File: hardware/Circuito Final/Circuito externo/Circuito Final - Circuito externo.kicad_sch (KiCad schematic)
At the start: 0 parts

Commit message: update circuito externo
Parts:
- added J1, J2: Conn_02x19_Odd_Even, Connector_PinSocket_2.54mm:PinSocket_2x19_P2.54mm_Vertical, symbol Connector_Generic:Conn_02x19_Odd_Even
- added J3, J4: Conn_01x02, Connector_PinSocket_2.54mm:PinSocket_1x02_P2.54mm_Vertical, symbol Connector_Generic:Conn_01x02
- added Jsalida_1, Jsalida_2, Jsalida_3, Jsalida_4, Jsalida_5: Conn_02x07_Odd_Even, Connector_IDC:IDC-Header_2x07_P2.54mm_Horizontal, symbol Connector_Generic:Conn_02x07_Odd_Even
- added SW1: SW_SPDT, symbol Switch:SW_SPDT
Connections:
- new net Bit_0: Jsalida_1.2 (Pin_2), Jsalida_2.2 (Pin_2), Jsalida_3.2 (Pin_2), Jsalida_4.2 (Pin_2), Jsalida_5.2 (Pin_2)
- new net Bit_1: Jsalida_1.1 (Pin_1), Jsalida_2.1 (Pin_1), Jsalida_3.1 (Pin_1), Jsalida_4.1 (Pin_1), Jsalida_5.1 (Pin_1)
- new net Bit_2: Jsalida_1.3 (Pin_3), Jsalida_2.3 (Pin_3), Jsalida_3.3 (Pin_3), Jsalida_4.3 (Pin_3), Jsalida_5.3 (Pin_3)
- new net Data_1: Jsalida_1.14 (Pin_14)
- new net Data_2: Jsalida_2.14 (Pin_14)
- new net Data_3: Jsalida_3.14 (Pin_14)
- new net Data_4: Jsalida_4.14 (Pin_14)
- new net Data_5: Jsalida_5.14 (Pin_14)
- new net GND: J1.19 (Pin_19), J1.21 (Pin_21), J1.7 (Pin_7), J3.2 (Pin_2), J4.2 (Pin_2), Jsalida_1.10 (Pin_10), Jsalida_2.10 (Pin_10), Jsalida_3.10 (Pin_10), Jsalida_4.10 (Pin_10), Jsalida_5.10 (Pin_10), SW1.3 (C)
- new net Vcc: J1.17 (Pin_17), SW1.2 (B)
- new net Vcc_out: Jsalida_1.13 (Pin_13), Jsalida_2.13 (Pin_13), Jsalida_3.13 (Pin_13), Jsalida_4.13 (Pin_13), Jsalida_5.13 (Pin_13), SW1.1 (A)
- new net bus_neg_1: Jsalida_1.7 (Pin_7), Jsalida_1.8 (Pin_8)
- new net bus_neg_2: Jsalida_2.7 (Pin_7), Jsalida_2.8 (Pin_8)
- new net bus_neg_3: Jsalida_3.7 (Pin_7), Jsalida_3.8 (Pin_8)
- new net bus_neg_4: Jsalida_4.7 (Pin_7), Jsalida_4.8 (Pin_8)
- new net bus_neg_5: Jsalida_5.7 (Pin_7), Jsalida_5.8 (Pin_8)
- new net bus_pos_1: Jsalida_1.5 (Pin_5), Jsalida_1.6 (Pin_6)
- new net bus_pos_2: Jsalida_2.5 (Pin_5), Jsalida_2.6 (Pin_6)
- new net bus_pos_3: Jsalida_3.5 (Pin_5), Jsalida_3.6 (Pin_6)
- new net bus_pos_4: Jsalida_4.5 (Pin_5), Jsalida_4.6 (Pin_6)
- new net bus_pos_5: Jsalida_5.5 (Pin_5), Jsalida_5.6 (Pin_6)
- new net clk_latch: Jsalida_1.11 (Pin_11), Jsalida_2.11 (Pin_11), Jsalida_3.11 (Pin_11), Jsalida_4.11 (Pin_11), Jsalida_5.11 (Pin_11)
- new net clk_shift: Jsalida_1.9 (Pin_9), Jsalida_2.9 (Pin_9), Jsalida_3.9 (Pin_9), Jsalida_4.9 (Pin_9), Jsalida_5.9 (Pin_9)
- new net reset: Jsalida_1.12 (Pin_12), Jsalida_2.12 (Pin_12), Jsalida_3.12 (Pin_12), Jsalida_4.12 (Pin_12), Jsalida_5.12 (Pin_12)
- new net salida_adc_1: Jsalida_1.4 (Pin_4)
- new net salida_adc_2: Jsalida_2.4 (Pin_4)
- new net salida_adc_3: Jsalida_3.4 (Pin_4)
- new net salida_adc_4: Jsalida_4.4 (Pin_4)
- new net salida_adc_5: Jsalida_5.4 (Pin_4)

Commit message: update pcb externo
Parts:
- removed Jsalida_5: Conn_02x07_Odd_Even, Connector_IDC:IDC-Header_2x07_P2.54mm_Horizontal, symbol Connector_Generic:Conn_02x07_Odd_Even
- added Bornera1: Conn_01x02_Socket, Huellas:TerminalBlock_bornier-2_P5.08mm, symbol Connector:Conn_01x02_Socket
- added C1: 10u, Capacitor_SMD:C_1206_3216Metric_Pad1.33x1.80mm_HandSolder, symbol Device:C
- added J5: Conn_02x04_Counter_Clockwise, Connector_PinHeader_2.54mm:PinHeader_2x04_P2.54mm_Vertical, symbol Connector_Generic:Conn_02x04_Counter_Clockwise
- added TP1, TP2: TestPoint, symbol Connector:TestPoint
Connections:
- net Bit_0: now also J2.1 (Pin_1)
- net Bit_1: now also J2.2 (Pin_2)
- net Bit_2: now also J2.4 (Pin_4)
- net Data_1: now also J1.4 (Pin_4)
- net Data_2: now also J1.24 (Pin_24)
- net GND: now also J1.20 (Pin_20), J2.10 (Pin_10), J2.19 (Pin_19), J2.31 (Pin_31)
- net bus_neg_1: now also Bornera1.1 (Pin_1), C1.2, TP2.1
- net bus_pos_1: now also J5.1 (Pin_1)
- net bus_pos_2: now also J5.2 (Pin_2)
- net bus_pos_3: now also J5.3 (Pin_3)
- net bus_pos_4: now also J5.4 (Pin_4)
- net clk_latch: now also J1.1 (Pin_1)
- net clk_shift: now also J1.2 (Pin_2)
- new net bus_pos_salida: Bornera1.2 (Pin_2), C1.1, J5.5 (Pin_5), J5.6 (Pin_6), J5.7 (Pin_7), J5.8 (Pin_8), TP1.1
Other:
- moved on the sheet: J1, J2, J3, J4, SW1

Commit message: version actualizada del pcb externo
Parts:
- removed J5: Conn_02x04_Counter_Clockwise, Connector_PinHeader_2.54mm:PinHeader_2x04_P2.54mm_Vertical, symbol Connector_Generic:Conn_02x04_Counter_Clockwise
- added SW2: SW_DIP_x04, Button_Switch_THT:SW_DIP_SPSTx04_Slide_9.78x12.34mm_W7.62mm_P2.54mm, symbol Switch:SW_DIP_x04
- SW1: footprint (none) -> Button_Switch_THT:SW_Slide_SPDT_Straight_CK_OS102011MS2Q
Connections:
- net Vcc: now also SW1.1 (A); no longer SW1.2 (B)
- net Vcc_out: now also SW1.2 (B); no longer SW1.1 (A)
- net bus_pos_1: now also SW2.1
- net bus_pos_2: now also SW2.2
- net bus_pos_3: now also SW2.3
- net bus_pos_4: now also SW2.4
- net bus_pos_salida: now also SW2.5, SW2.6, SW2.7, SW2.8
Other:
- moved on the sheet: SW1

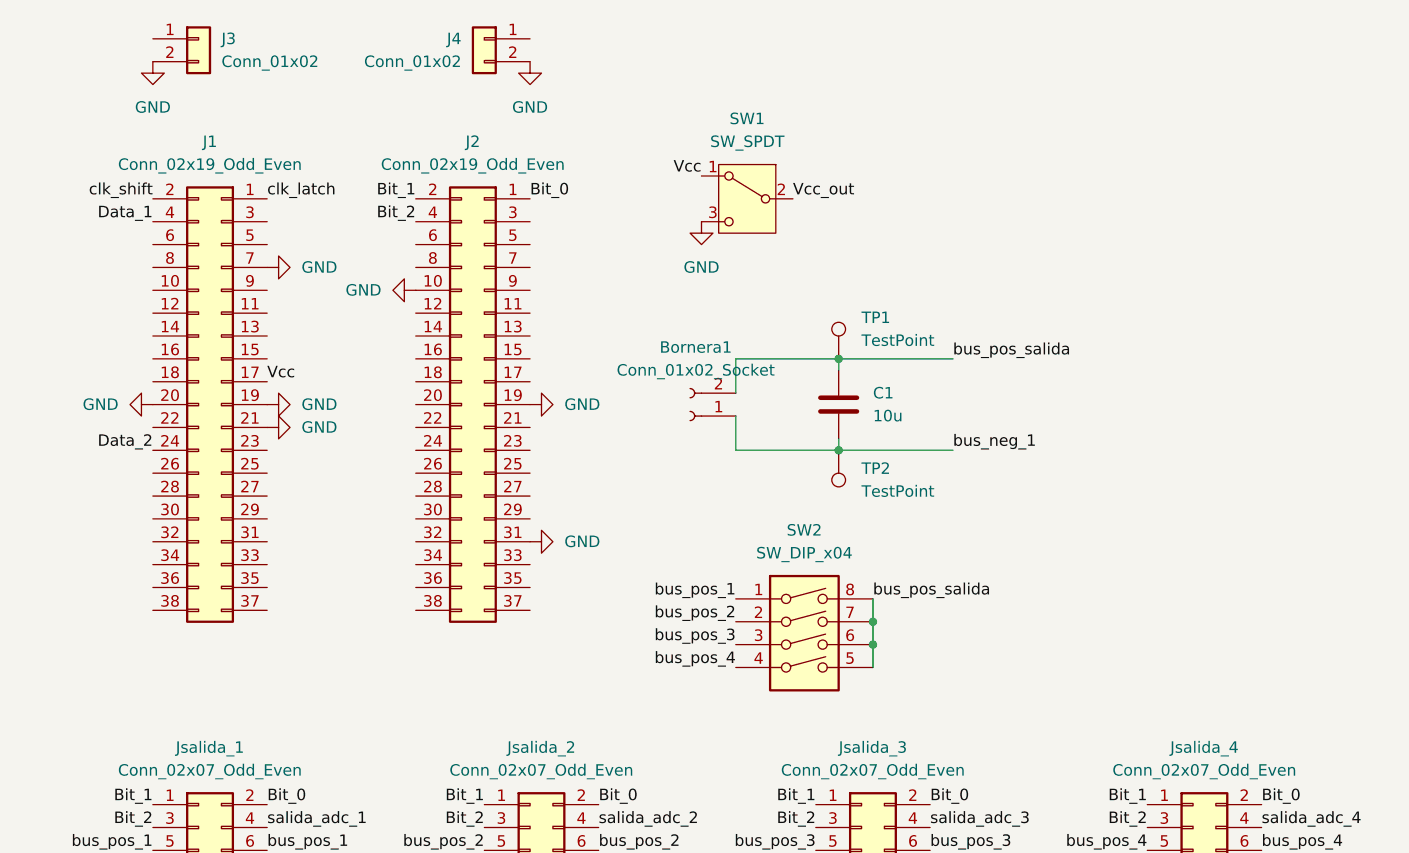
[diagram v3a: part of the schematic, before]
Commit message: update pcb circuito externo
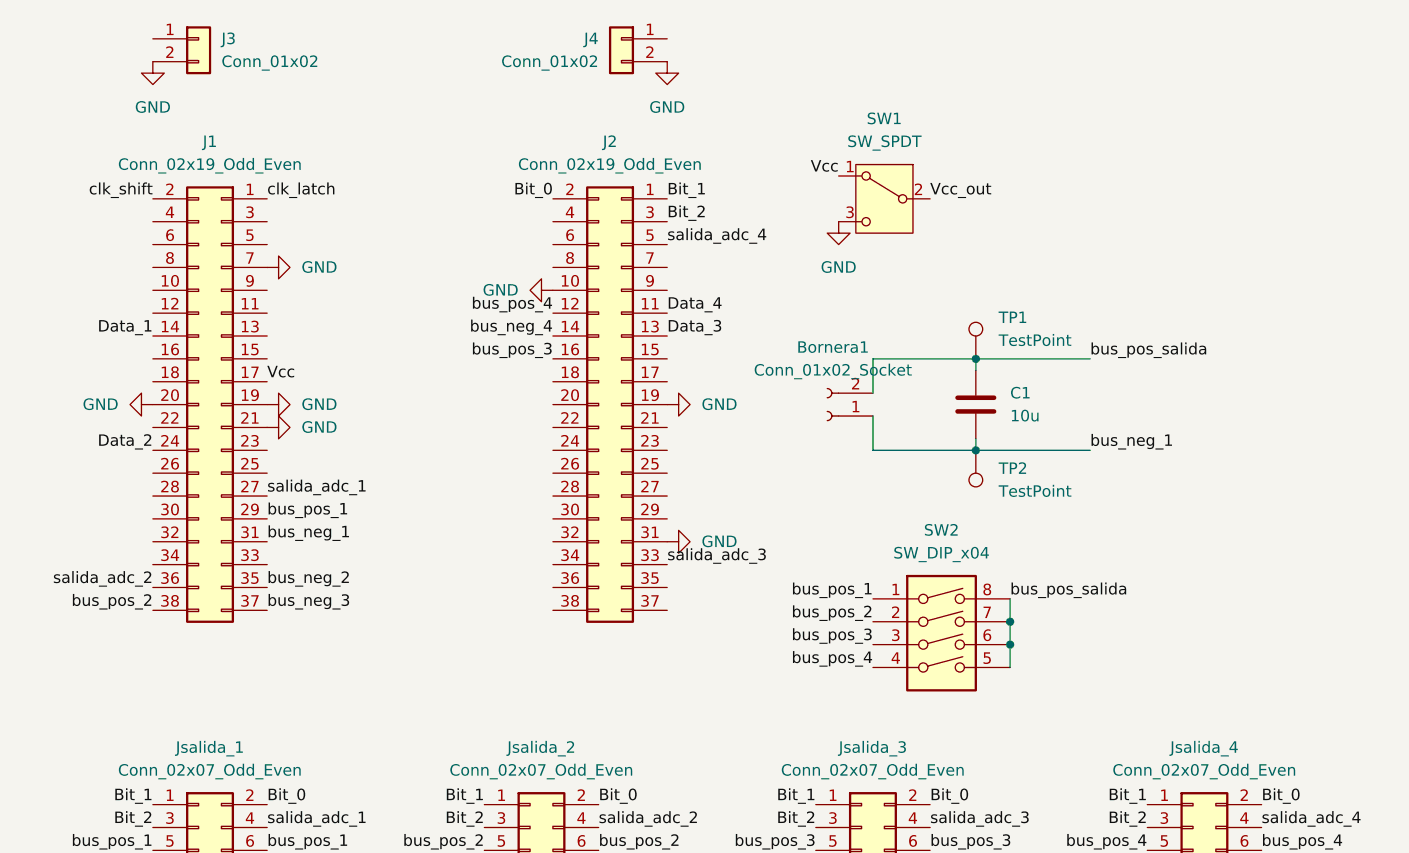
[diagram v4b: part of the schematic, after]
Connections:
- net Bit_0: now also J2.2 (Pin_2); no longer J2.1 (Pin_1)
- net Bit_1: now also J2.1 (Pin_1); no longer J2.2 (Pin_2)
- net Bit_2: now also J2.3 (Pin_3); no longer J2.4 (Pin_4)
- net Data_1: now also J1.14 (Pin_14); no longer J1.4 (Pin_4)
- net Data_3: now also J2.13 (Pin_13)
- net Data_4: now also J2.11 (Pin_11)
- net bus_neg_1: now also J1.31 (Pin_31)
- net bus_neg_2: now also J1.35 (Pin_35)
- net bus_neg_3: now also J1.37 (Pin_37)
- net bus_neg_4: now also J2.14 (Pin_14)
- net bus_pos_1: now also J1.29 (Pin_29)
- net bus_pos_2: now also J1.38 (Pin_38)
- net bus_pos_3: now also J2.16 (Pin_16)
- net bus_pos_4: now also J2.12 (Pin_12)
- net salida_adc_1: now also J1.27 (Pin_27)
- net salida_adc_2: now also J1.36 (Pin_36)
- net salida_adc_3: now also J2.33 (Pin_33)
- net salida_adc_4: now also J2.5 (Pin_5)
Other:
- moved on the sheet: Bornera1, C1, J2, J4, SW1, SW2, TP1, TP2

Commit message: subida spice del cir central (divisor resistivo)
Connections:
- net bus_neg_2: no longer Jsalida_2.7 (Pin_7), Jsalida_2.8 (Pin_8)
- net bus_neg_3: no longer Jsalida_3.7 (Pin_7), Jsalida_3.8 (Pin_8)
- net bus_neg_4: no longer Jsalida_4.7 (Pin_7), Jsalida_4.8 (Pin_8)
- net bus_pos_1: now also Jsalida_2.7 (Pin_7), Jsalida_2.8 (Pin_8)
- net bus_pos_2: now also Jsalida_3.7 (Pin_7), Jsalida_3.8 (Pin_8)
- net bus_pos_3: now also Jsalida_4.7 (Pin_7), Jsalida_4.8 (Pin_8)
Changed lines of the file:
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@@
+		)
+	)
+	(label "bus_pos_2"
+		(at 116.84 147.32 180)
+		(effects
+			(font
+				(size 1.27 1.27)
+			)
+			(justify right bottom)
 		)
 	)
@@
 		)
 	)
+	(label "bus_pos_3"
+		(at 166.37 147.32 0)
+		(effects
+			(font
+				(size 1.27 1.27)
+			)
+			(justify left bottom)
+		)
+	)
 	(label "Bit_0"
 		(at 166.37 139.7 0)
@@
 		)
 	)
-	(label "bus_neg_2"
-		(at 80.01 147.32 180)
-		(effects
-			(font
-				(size 1.27 1.27)
-			)
-			(justify right bottom)
-		)
-	)
 	(label "bus_pos_1"
 		(at 55.88 107.95 0)
@@
 		)
 	)
+	(label "bus_pos_1"
+		(at 80.01 147.32 180)
+		(effects
+			(font
+				(size 1.27 1.27)
+			)
+			(justify right bottom)
+		)
+	)
 	(label "Bit_1"
 		(at 100.33 72.39 0)
@@
 		)
 	)
-	(label "bus_neg_4"
-		(at 153.67 147.32 180)
-		(effects
-			(font
-				(size 1.27 1.27)
-			)
-			(justify right bottom)
-		)
-	)
 	(label "Vcc_out"
 		(at 129.54 72.39 0)
@@
 		)
 	)
-	(label "bus_neg_3"
-		(at 129.54 147.32 0)
-		(effects
-			(font
-				(size 1.27 1.27)
-			)
-			(justify left bottom)
-		)
-	)
 	(label "bus_pos_salida"
 		(at 147.32 90.17 0)
@@
 	)
 	(label "bus_neg_2"
-		(at 92.71 147.32 0)
-		(effects
-			(font
-				(size 1.27 1.27)
-			)
-			(justify left bottom)
-		)
-	)
-	(label "bus_neg_2"
 		(at 55.88 115.57 0)
 		(effects
@@
 		)
 	)
-	(label "bus_neg_3"
-		(at 116.84 147.32 180)
-		(effects
-			(font
-				(size 1.27 1.27)
-			)
-			(justify right bottom)
-		)
-	)
 	(label "reset"
 		(at 166.37 152.4 0)
@@
 		)
 	)
+	(label "bus_pos_3"
+		(at 153.67 147.32 180)
+		(effects
+			(font
+				(size 1.27 1.27)
+			)
+			(justify right bottom)
+		)
+	)
+	(label "bus_pos_1"
+		(at 92.71 147.32 0)
+		(effects
+			(font
+				(size 1.27 1.27)
+			)
+			(justify left bottom)
+		)
+	)
 	(label "bus_neg_1"
 		(at 55.88 110.49 0)
@@
 		)
 	)
-	(label "bus_neg_4"
-		(at 166.37 147.32 0)
-		(effects
-			(font
-				(size 1.27 1.27)
-			)
-			(justify left bottom)
-		)
-	)
 	(label "bus_pos_4"
 		(at 166.37 144.78 0)
@@
 		(effects
 			(font
+				(size 1.27 1.27)
+			)
+			(justify left bottom)
+		)
+	)
+	(label "bus_pos_2"
+		(at 129.54 147.32 0)
+		(effects
+			(font

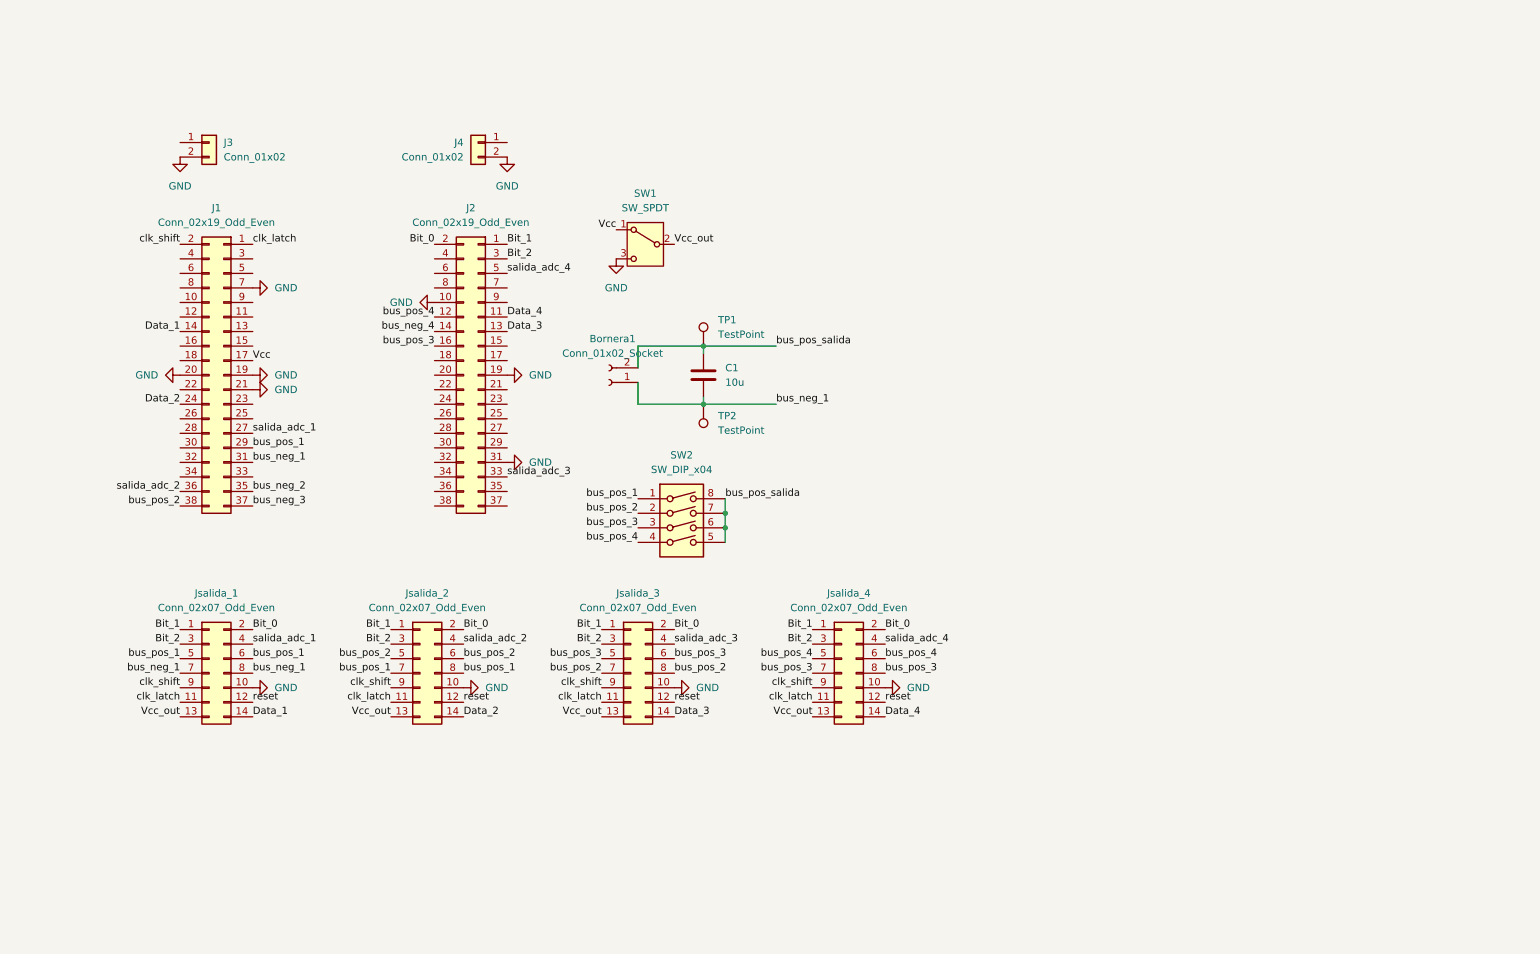
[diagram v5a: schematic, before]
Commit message: update de bitacora, valores de resistores del divisor en spice e implementacion en el kicad del circuito externo
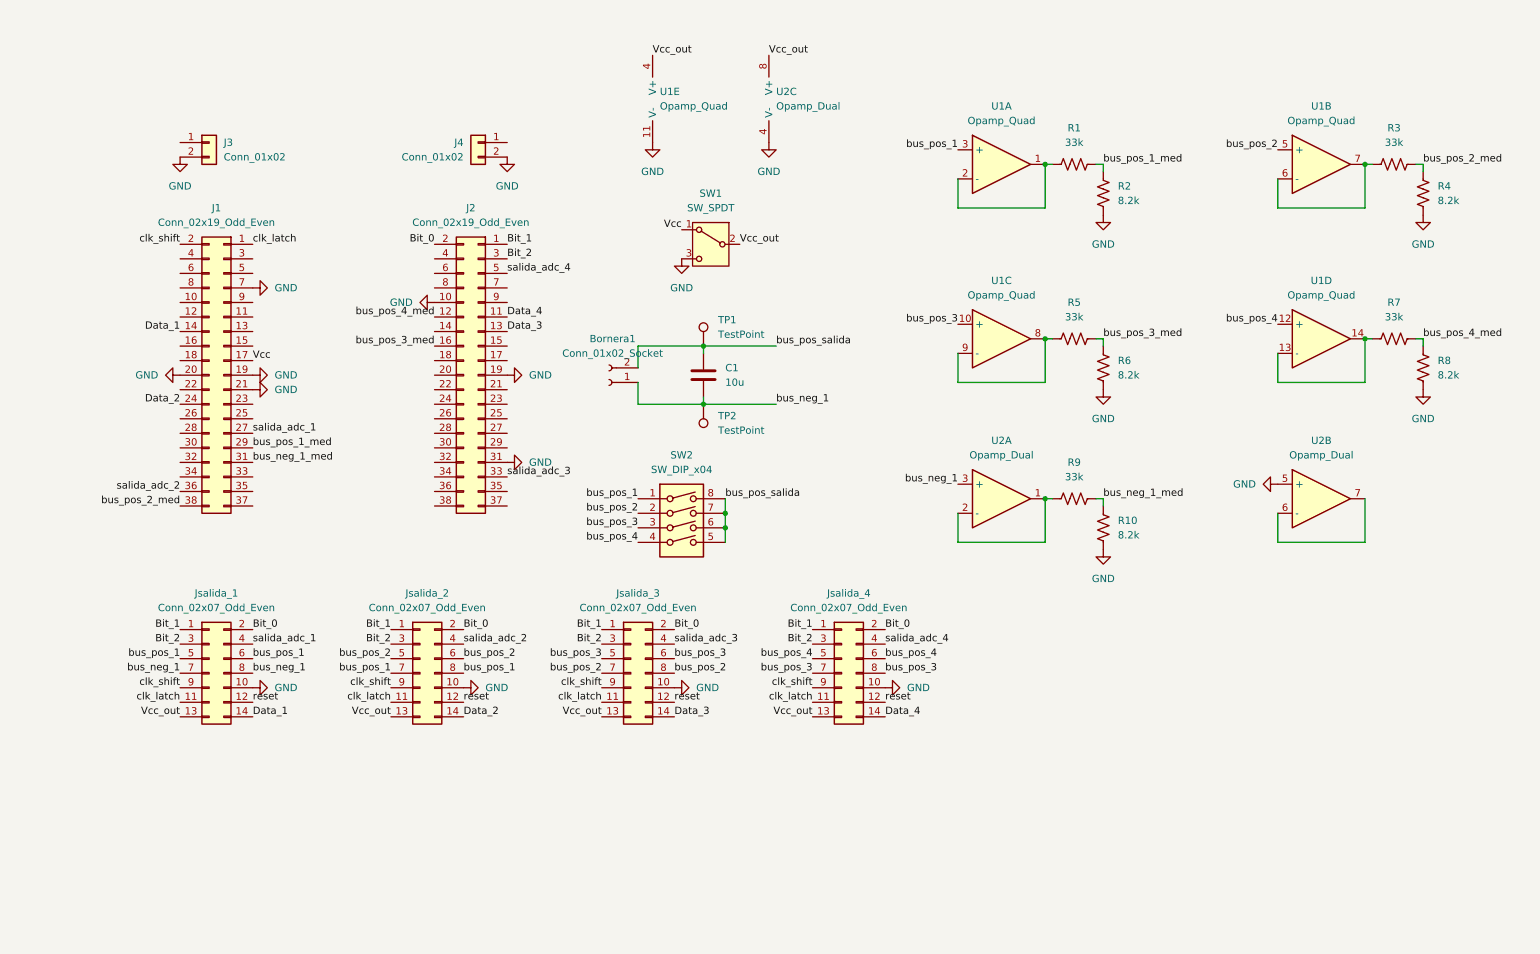
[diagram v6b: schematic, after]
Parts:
- added R1, R3, R5, R7, R9: 33k, symbol Device:R_US
- added R10, R2, R4, R6, R8: 8.2k, symbol Device:R_US
- added U1: Opamp_Quad, symbol Device:Opamp_Quad
- added U2: Opamp_Dual, symbol Device:Opamp_Dual
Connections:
- net GND: now also R10.1, R2.1, R4.1, R6.1, R8.1, U1.11 (V-), U2.4 (V-), U2.5 (+)
- net Vcc_out: now also U1.4 (V+), U2.8 (V+)
- net bus_neg_1: now also U2.3 (+); no longer J1.31 (Pin_31)
- net bus_pos_1: now also U1.3 (+); no longer J1.29 (Pin_29)
- net bus_pos_2: now also U1.5 (+); no longer J1.38 (Pin_38)
- net bus_pos_3: now also U1.10 (+); no longer J2.16 (Pin_16)
- net bus_pos_4: now also U1.12 (+); no longer J2.12 (Pin_12)
- net bus_neg_2: no longer names the net of J1.35 (Pin_35)
- net bus_neg_3: no longer names the net of J1.37 (Pin_37)
- net bus_neg_4: no longer names the net of J2.14 (Pin_14)
- new net: R5.1, U1.8, U1.9 (-)
- new net: R3.1, U1.6 (-), U1.7
- new net: U2.6 (-), U2.7
- new net: R7.1, U1.13 (-), U1.14
- new net: R1.1, U1.1, U1.2 (-)
- new net: R9.1, U2.1, U2.2 (-)
- new net bus_neg_1_med: J1.31 (Pin_31), R10.2, R9.2
- new net bus_pos_1_med: J1.29 (Pin_29), R1.2, R2.2
- new net bus_pos_2_med: J1.38 (Pin_38), R3.2, R4.2
- new net bus_pos_3_med: J2.16 (Pin_16), R5.2, R6.2
- new net bus_pos_4_med: J2.12 (Pin_12), R7.2, R8.2
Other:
- moved on the sheet: SW1
